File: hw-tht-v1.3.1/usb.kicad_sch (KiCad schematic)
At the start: 7 parts, among them J11 USB-A or USB-C, U12 USBLC6-2SC6

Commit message: THT rev B: dual USB-A/USB-C footprint, unrouted v1.3.1 board
- J11 footprint USB_A_C_Dual_Molex_67643_GCT_USB4085_Horizontal: Molex 67643
  USB-A or GCT USB4085 USB-C (all THT), both centred on one line, front faces
  1.5 mm beyond the board edge
- project rules: min hole-to-hole 0.45 mm, min annular 0.12 mm for the
  USB4085 pins; PicoGUS-THT.kicad_dru keeps 0.50/0.13 mm everywhere else
- PicoGUS-THT.kicad_pcb: unrouted (tracks, vias and zone fills removed),
  v1.3.0 positions; U1 on RPi_Pico_SMD_TH_USB, U3/U4 on the nested footprint
  at their old centres (turned 90 deg), new parts parked below the ISA edge,
  J11 aligned to the bracket edge line; silkscreen v1.3.1
- schematic: J11 footprint, F1 Bourns MF-R050

Still to come: BOM, socket BOM, README.

Co-Authored-By: Claude Opus 5.5 <noreply@anthropic.com>
Claude-Session: https://claude.ai/code/session_011utN3x8yYUNDvkpGCEq5yD
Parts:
- F1: footprint Fuse:Fuse_Bourns_MF-RG050 -> Fuse:Fuse_Bourns_MF-RHT050; LCSC TBD -> C208476
- J11: footprint PiGUS library:USB_A_C_Dual -> PiGUS library:USB_A_C_Dual_Molex_67643_GCT_USB4085_Horizontal; Alternatives USB-C: TBD -> USB-C: GCT USB4085-GF-A (DK 2073-USB4085-GF-ACT-ND, LCSC C7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; DigiKey WM11258-ND -> WM4993-ND; LCSC TBD -> C2798029; MPN 0676432910 -> 0676430910
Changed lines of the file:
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@@
 			)
 		)
-		(property "Footprint" "PiGUS library:USB_A_C_Dual"
-			(at 76.2 101.6 0)
-			(hide yes)
-			(show_name no)
-			(do_not_autoplace no)
-			(effects
-				(font
-					(size 1.27 1.27)
-				)
-			)
-		)
-		(property "Datasheet" ""
-			(at 76.2 101.6 0)
-			(hide yes)
-			(show_name no)
-			(do_not_autoplace no)
-			(effects
-				(font
-					(size 1.27 1.27)
-				)
-			)
-		)
-		(property "Description" "USB host receptacle at the bracket: fit a USB-A or a USB-C socket"
+		(property "Footprint" "PiGUS library:USB_A_C_Dual_Molex_67643_GCT_USB4085_Horizontal"
+			(at 76.2 101.6 0)
+			(hide yes)
+			(show_name no)
+			(do_not_autoplace no)
+			(effects
+				(font
+					(size 1.27 1.27)
+				)
+			)
+		)
+		(property "Datasheet" "https://gct.co/files/drawings/usb4085.pdf"
+			(at 76.2 101.6 0)
+			(hide yes)
+			(show_name no)
+			(do_not_autoplace no)
+			(effects
+				(font
+					(size 1.27 1.27)
+				)
+			)
+		)
+		(property "Description" "USB host receptacle at the bracket, one footprint: fit a USB-A (Molex 67643) OR a USB-C (GCT USB4085) socket"
 			(at 76.2 101.6 0)
 			(hide yes)
@@
 			)
 		)
-		(property "MPN" "0676432910"
-			(at 76.2 101.6 0)
-			(hide yes)
-			(show_name no)
-			(do_not_autoplace no)
-			(effects
-				(font
-					(size 1.27 1.27)
-				)
-			)
-		)
-		(property "DigiKey" "WM11258-ND"
-			(at 76.2 101.6 0)
-			(hide yes)
-			(show_name no)
-			(do_not_autoplace no)
-			(effects
-				(font
-					(size 1.27 1.27)
-				)
-			)
-		)
-		(property "LCSC" "TBD"
-			(at 76.2 101.6 0)
-			(hide yes)
-			(show_name no)
-			(do_not_autoplace no)
-			(effects
-				(font
-					(size 1.27 1.27)
-				)
-			)
-		)
-		(property "Alternatives" "USB-C: TBD"
+		(property "MPN" "0676430910"
+			(at 76.2 101.6 0)
+			(hide yes)
+			(show_name no)
+			(do_not_autoplace no)
+			(effects
+				(font
+					(size 1.27 1.27)
+				)
+			)
+		)
+		(property "DigiKey" "WM4993-ND"
+			(at 76.2 101.6 0)
+			(hide yes)
+			(show_name no)
+			(do_not_autoplace no)
+			(effects
+				(font
+					(size 1.27 1.27)
+				)
+			)
+		)
+		(property "LCSC" "C2798029"
+			(at 76.2 101.6 0)
+			(hide yes)
+			(show_name no)
+			(do_not_autoplace no)
+			(effects
+				(font
+					(size 1.27 1.27)
+				)
+			)
+		)
+		(property "Alternatives" "USB-C: GCT USB4085-GF-A (DK 2073-USB4085-GF-ACT-ND, LCSC C7095263). USB-A white: Molex 0676433910 (DK WM14667-ND)"
 			(at 76.2 101.6 0)
 			(hide yes)
@@
 			)
 		)
-		(property "Footprint" "Fuse:Fuse_Bourns_MF-RG050"
+		(property "Footprint" "Fuse:Fuse_Bourns_MF-RHT050"
 			(at 101.6 73.66 0)
 			(hide yes)
@@
 			)
 		)
-		(property "Description" "Resettable fuse, 0.5 A hold, radial"
+		(property "Description" "Resettable fuse (PTC), 0.5 A hold / 1 A trip, 60 V, radial 7.9 mm disc, 5.1 mm lead spacing (USB VBUS)"
 			(at 101.6 73.66 0)
 			(hide yes)
@@
 			)
 		)
-		(property "LCSC" "TBD"
-			(at 101.6 73.66 0)
-			(hide yes)
+		(property "LCSC" "C208476"
+			(at 101.6 73.66 0)
+			(hide yes)

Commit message: THT rev B: review fixes, C34 220uF, schematic PDF
Schematic
- C34 (USB VBUS bulk) 220 uF low-impedance Rubycon 16ZLH220MEFC6.3X11
  (USB 2.0 asks for >= 120 uF per host port)
- own UUID namespace for the rev B items (the USB sheet had reused UUIDs of
  v1.3.0 items, which mixed up ERC markers)
- TP1-TP3 pin names empty ("") in the embedded Pico_USB copy (KiCad 10 drew
  "~" literally)
- R25/R26 DigiKey/LCSC fields, U3/U4 adapter note (PA0034C first, BOB-13994
  has 0.635 mm pads), U12 in the title block's SMD list, USB sheet note
  reworded, USB-C always-on VBUS warning
- schematic PDF re-exported (4 pages)

Board
- U1: the library footprint's Pico pin-name/SWD silkscreen texts removed
  again (as in the v1.3.0 label clean-up)
- U3/U4 references back at their v1.3.0 spots (were on the gold fingers)
- U1, U3, U4 back in their footprint groups
- VBUS_USB in the pwr net class

BOM: C34 own line; BOM, uploads and socket BOM regenerated.

Co-Authored-By: Claude Opus 5.5 <noreply@anthropic.com>
Claude-Session: https://claude.ai/code/session_011utN3x8yYUNDvkpGCEq5yD
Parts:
- C34: value 47uF -> 220uF; footprint Capacitor_THT:CP_Radial_D5.0mm_P2.00mm -> Capacitor_THT:CP_Radial_D6.3mm_P2.50mm; DigiKey 1189-2919-ND -> 1189-1726-ND; LCSC C88761 -> C338177; MPN 35YXJ47M5X11 -> 16ZLH220MEFC6.3X11
- R25, R26: DigiKey 56.0KXBK-ND -> MFR-25FBF52-56K-ND; LCSC TBD -> C127224 (CCO MF1/4W-56K 1%)
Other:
- note added: "Data straight from the Pico's USB test points TP3 (D+) / TP2 (D-) (U1, sheet 1), behind the 27R series resistors on the Pico module. The Pico must be soldered FLAT on the board (castellated edge or through-hole pins, no header) so TP1-TP3 can be soldered from the back of the card. With the Pico on headers or in a socket the TP pads do not reach the card: wire TP1-TP3 to the holes, or use a micro-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"
- note removed: "Data straight from the Pico's USB test points TP3 (D+) / TP2 (D-), behind the Pico's own 27R series resistors (sheet 1). The Pico must be soldered FLAT on the board (castellated edge or through-hole pins, no header) so TP1-TP3 can be soldered from the back of the card. With the Pico on headers or in a socket the port is unusable: use a micro-USB OTG adapter on the Pico (with jumper J7) instead, a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"
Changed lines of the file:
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@@
 		(instances
 			(project "PicoGUS-THT"
-				(path "/8fb4b197-630e-4faa-9892-8ecaeb71c13b/2aef9491-1bd6-5c71-9def-f52d07b96cdf"
+				(path "/8fb4b197-630e-4faa-9892-8ecaeb71c13b/6a46ae49-e7e4-5a48-8b33-ff41e9c8fc77"
 					(reference "J11")
 					(unit 1)
@@
 			)
 		)
-		(property "Description" "Resettable fuse (PTC), 0.5 A hold / 1 A trip, 60 V, radial 7.9 mm disc, 5.1 mm lead spacing (USB VBUS)"
+		(property "Description" "Resettable fuse (PTC), 0.5 A hold / 1 A trip, 60 V, radial 7.9 mm disc, 5.1 mm lead spacing, up to 13.7 mm tall (USB VBUS)"
 			(at 101.6 73.66 0)
 			(hide yes)
@@
 		(instances
 			(project "PicoGUS-THT"
-				(path "/8fb4b197-630e-4faa-9892-8ecaeb71c13b/2aef9491-1bd6-5c71-9def-f52d07b96cdf"
+				(path "/8fb4b197-630e-4faa-9892-8ecaeb71c13b/6a46ae49-e7e4-5a48-8b33-ff41e9c8fc77"
 					(reference "F1")
 					(unit 1)
@@
 		(instances
 			(project "PicoGUS-THT"
-				(path "/8fb4b197-630e-4faa-9892-8ecaeb71c13b/2aef9491-1bd6-5c71-9def-f52d07b96cdf"
+				(path "/8fb4b197-630e-4faa-9892-8ecaeb71c13b/6a46ae49-e7e4-5a48-8b33-ff41e9c8fc77"
 					(reference "#PWR0200")
 					(unit 1)
@@
 		(instances
 			(project "PicoGUS-THT"
-				(path "/8fb4b197-630e-4faa-9892-8ecaeb71c13b/2aef9491-1bd6-5c71-9def-f52d07b96cdf"
+				(path "/8fb4b197-630e-4faa-9892-8ecaeb71c13b/6a46ae49-e7e4-5a48-8b33-ff41e9c8fc77"
 					(reference "#FLG106")
 					(unit 1)
@@
 			)
 		)
-		(property "DigiKey" "56.0KXBK-ND"
+		(property "DigiKey" "MFR-25FBF52-56K-ND"
 			(at 116.84 90.17 0)
 			(hide yes)
@@
 			)
 		)
-		(property "LCSC" "TBD"
+		(property "LCSC" "C127224 (CCO MF1/4W-56K 1%)"
 			(at 116.84 90.17 0)
 			(hide yes)
@@
 		(instances
 			(project "PicoGUS-THT"
-				(path "/8fb4b197-630e-4faa-9892-8ecaeb71c13b/2aef9491-1bd6-5c71-9def-f52d07b96cdf"
+				(path "/8fb4b197-630e-4faa-9892-8ecaeb71c13b/6a46ae49-e7e4-5a48-8b33-ff41e9c8fc77"
 					(reference "R25")
 					(unit 1)
@@
 			)
 		)
-		(property "DigiKey" "56.0KXBK-ND"
+		(property "DigiKey" "MFR-25FBF52-56K-ND"
 			(at 124.46 90.17 0)
 			(hide yes)
@@
 			)
 		)
-		(property "LCSC" "TBD"
+		(property "LCSC" "C127224 (CCO MF1/4W-56K 1%)"
 			(at 124.46 90.17 0)
 			(hide yes)
@@
 		(instances
 			(project "PicoGUS-THT"
-				(path "/8fb4b197-630e-4faa-9892-8ecaeb71c13b/2aef9491-1bd6-5c71-9def-f52d07b96cdf"
+				(path "/8fb4b197-630e-4faa-9892-8ecaeb71c13b/6a46ae49-e7e4-5a48-8b33-ff41e9c8fc77"
 					(reference "R26")
 					(unit 1)
@@
 		(instances
 			(project "PicoGUS-THT"
-				(path "/8fb4b197-630e-4faa-9892-8ecaeb71c13b/2aef9491-1bd6-5c71-9def-f52d07b96cdf"
+				(path "/8fb4b197-630e-4faa-9892-8ecaeb71c13b/6a46ae49-e7e4-5a48-8b33-ff41e9c8fc77"
 					(reference "#PWR0201")
 					(unit 1)
@@
 			)
 		)
-		(property "Value" "47uF"
+		(property "Value" "220uF"
 			(at 144.145 91.44 0)
 			(show_name no)
@@
 			)
 		)
-		(property "Footprint" "Capacitor_THT:CP_Radial_D5.0mm_P2.00mm"
+		(property "Footprint" "Capacitor_THT:CP_Radial_D6.3mm_P2.50mm"
 			(at 142.24 90.17 0)
 			(hide yes)
@@
 			)
 		)
-		(property "Description" "47uF 35V aluminium electrolytic, 5mm dia, 2mm pitch (USB VBUS bulk)"
+		(property "Description" "220uF 16V low-impedance aluminium electrolytic, 6.3 mm dia, 2.5 mm pitch (USB VBUS bulk, >= 120uF per USB 2.0)"
 			(at 142.24 90.17 0)
 			(hide yes)
@@
 			)
 		)
-		(property "MPN" "35YXJ47M5X11"
+		(property "MPN" "16ZLH220MEFC6.3X11"
 			(at 142.24 90.17 0)
 			(hide yes)
@@
 			)
 		)
-		(property "DigiKey" "1189-2919-ND"
+		(property "DigiKey" "1189-1726-ND"
 			(at 142.24 90.17 0)
 			(hide yes)
@@
 			)
 		)
-		(property "LCSC" "C88761"
+		(property "LCSC" "C338177"
 			(at 142.24 90.17 0)
 			(hide yes)
@@
 		(instances
 			(project "PicoGUS-THT"
-				(path "/8fb4b197-630e-4faa-9892-8ecaeb71c13b/2aef9491-1bd6-5c71-9def-f52d07b96cdf"
+				(path "/8fb4b197-630e-4faa-9892-8ecaeb71c13b/6a46ae49-e7e4-5a48-8b33-ff41e9c8fc77"
 					(reference "C34")
 					(unit 1)
@@
 		(instances
 			(project "PicoGUS-THT"
-				(path "/8fb4b197-630e-4faa-9892-8ecaeb71c13b/2aef9491-1bd6-5c71-9def-f52d07b96cdf"
+				(path "/8fb4b197-630e-4faa-9892-8ecaeb71c13b/6a46ae49-e7e4-5a48-8b33-ff41e9c8fc77"
 					(reference "#PWR0202")
 					(unit 1)
@@
 		(instances
 			(project "PicoGUS-THT"
-				(path "/8fb4b197-630e-4faa-9892-8ecaeb71c13b/2aef9491-1bd6-5c71-9def-f52d07b96cdf"
+				(path "/8fb4b197-630e-4faa-9892-8ecaeb71c13b/6a46ae49-e7e4-5a48-8b33-ff41e9c8fc77"
 					(reference "C35")
 					(unit 1)
@@
 		(instances
 			(project "PicoGUS-THT"
-				(path "/8fb4b197-630e-4faa-9892-8ecaeb71c13b/2aef9491-1bd6-5c71-9def-f52d07b96cdf"
+				(path "/8fb4b197-630e-4faa-9892-8ecaeb71c13b/6a46ae49-e7e4-5a48-8b33-ff41e9c8fc77"
 					(reference "#PWR0203")
 					(unit 1)
@@
 		(instances
 			(project "PicoGUS-THT"
-				(path "/8fb4b197-630e-4faa-9892-8ecaeb71c13b/2aef9491-1bd6-5c71-9def-f52d07b96cdf"
+				(path "/8fb4b197-630e-4faa-9892-8ecaeb71c13b/6a46ae49-e7e4-5a48-8b33-ff41e9c8fc77"
 					(reference "U12")
 					(unit 1)
@@
 		(instances
 			(project "PicoGUS-THT"
-				(path "/8fb4b197-630e-4faa-9892-8ecaeb71c13b/2aef9491-1bd6-5c71-9def-f52d07b96cdf"
+				(path "/8fb4b197-630e-4faa-9892-8ecaeb71c13b/6a46ae49-e7e4-5a48-8b33-ff41e9c8fc77"
 					(reference "#PWR0204")
 					(unit 1)
@@
 		)
 	)
-	(text "Data straight from the Pico's USB test points TP3 (D+) / TP2 (D-), behind the Pico's own 27R\nseries resistors (sheet 1). The Pico must be soldered FLAT on the board (castellated edge or\nthrough-hole pins, no header) so TP1-TP3 can be soldered from the back of the card.\nWith the Pico on headers or in a socket the port is unusable: use a micro-USB OTG adapter\non the Pico (with jumper J7) instead, as on v1.3.0. Never use both at the same time.\nVBUS from ISA +5V via F1 (resettable, 0.5 A hold). The Pico VBUS pin is not used for this port.\nJ11 takes a USB-A OR a USB-C receptacle. R25/R26 (Rp 56k = default USB power) tell a USB-C\ndevice that this is a 5 V source; with a USB-A socket they are not connected (fit them anyway).\nU12 (ESD array, SOT-23-6) is optional."
+	(text "Data straight from the Pico's USB test points TP3 (D+) / TP2 (D-) (U1, sheet 1), behind the 27R\nseries resistors on the Pico module. The Pico must be soldered FLAT on the board (castellated edge or\nthrough-hole pins, no header) so TP1-TP3 can be soldered from the back of the card.\nWith the Pico on headers or in a socket the TP pads do not reach the card: wire TP1-TP3 to the holes,\nor use a micro-USB OTG adapter on the Pico (with jumper J7) as on v1.3.0. Never use both at once.\nVBUS from ISA +5V via F1 (resettable, 0.5 A hold). The Pico VBUS pin is not used for this port.\nJ11 takes a USB-A OR a USB-C receptacle. R25/R26 (Rp 56k = default USB power) tell a USB-C\ndevice that this is a 5 V source; with a USB-A socket they are not connected (fit them anyway).\nUSB-C: VBUS is always on (no \"cold socket\"), so never connect J11 to another 5 V source (charger, PC).\nU12 (ESD array, SOT-23-6) is optional."
 		(exclude_from_sim no)
 		(at 63.5 134.62 0)

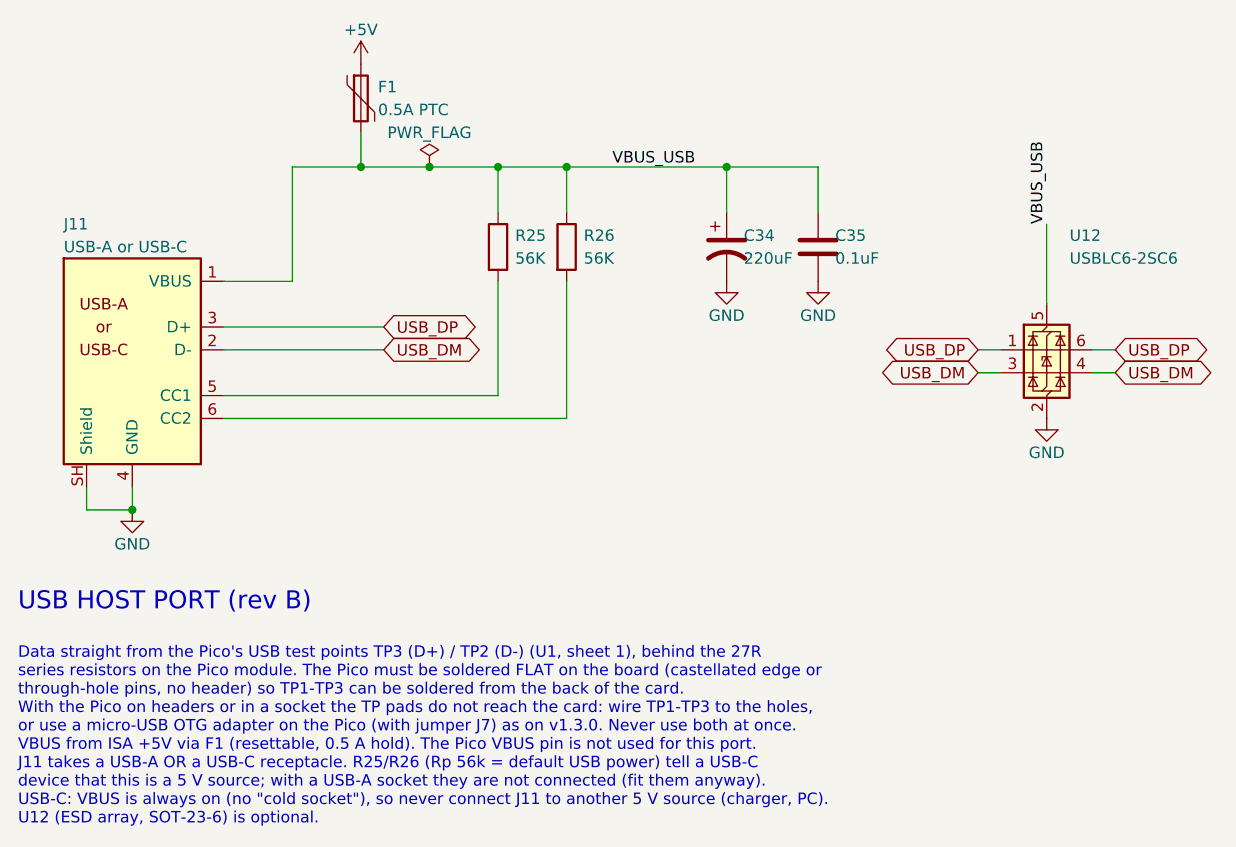
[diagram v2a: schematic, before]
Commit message: THT rev B: USB-A only for J11 (USB-C on hold)
- J11: Connector:USB_A on the stock Connector_USB:USB_A_Molex_67643_Horizontal
  (Molex 0676430910), parked with the flange 1.5 mm beyond the bracket edge
- R25/R26 (USB-C CC Rp) removed; design rules back to v1.3.0 (min hole-to-hole
  0.50 mm, annular 0.13 mm), PicoGUS-THT.kicad_dru removed
- the dual USB-A/USB-C footprint stays in the shared library, unused, for a
  possible USB-C option later
- BOM, DigiKey uploads, schematic PDF and README updated

Co-Authored-By: Claude Opus 5.5 <noreply@anthropic.com>
Claude-Session: https://claude.ai/code/session_011utN3x8yYUNDvkpGCEq5yD
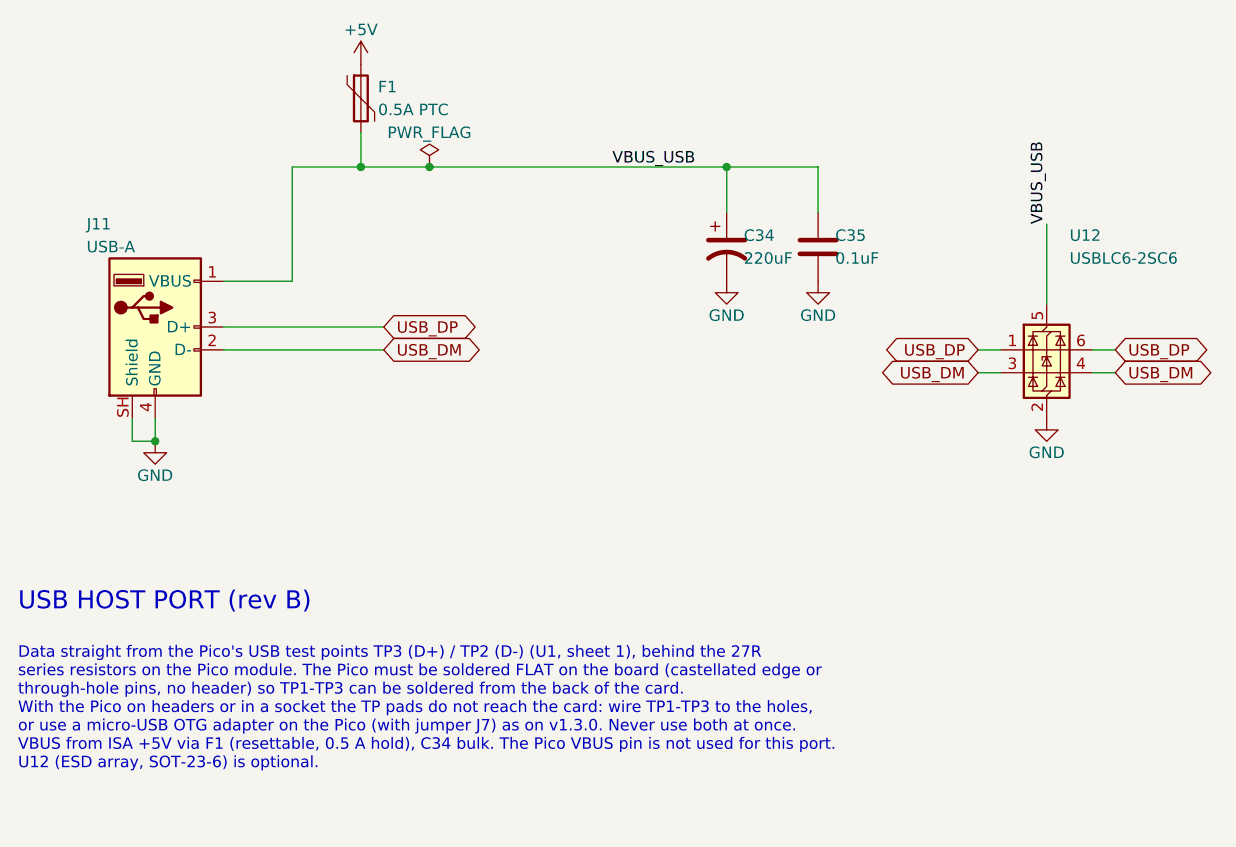
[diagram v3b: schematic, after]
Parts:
- removed R25, R26: 56K, Resistor_THT:R_Axial_DIN0207_L6.3mm_D2.5mm_P10.16mm_Horizontal, symbol Device:R
- J11: value USB-A or USB-C -> USB-A; footprint PiGUS library:USB_A_C_Dual_Molex_67643_GCT_USB4085_Horizontal -> Connector_USB:USB_A_Molex_67643_Horizontal; symbol PiGUS library:USB_A_C_Dual -> Connector:USB_A; Alternatives USB-C: GCT USB4085-GF-A (DK 2073-USB4085-GF-ACT-ND, LCSC C7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 -> Molex 0676433910 (white, DK WM14667-ND); 0676432910 (DK WM1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
